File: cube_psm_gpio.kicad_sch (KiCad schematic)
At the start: 2 parts, among them J1 DF17_1.0H_-80DP-0.5V_57_

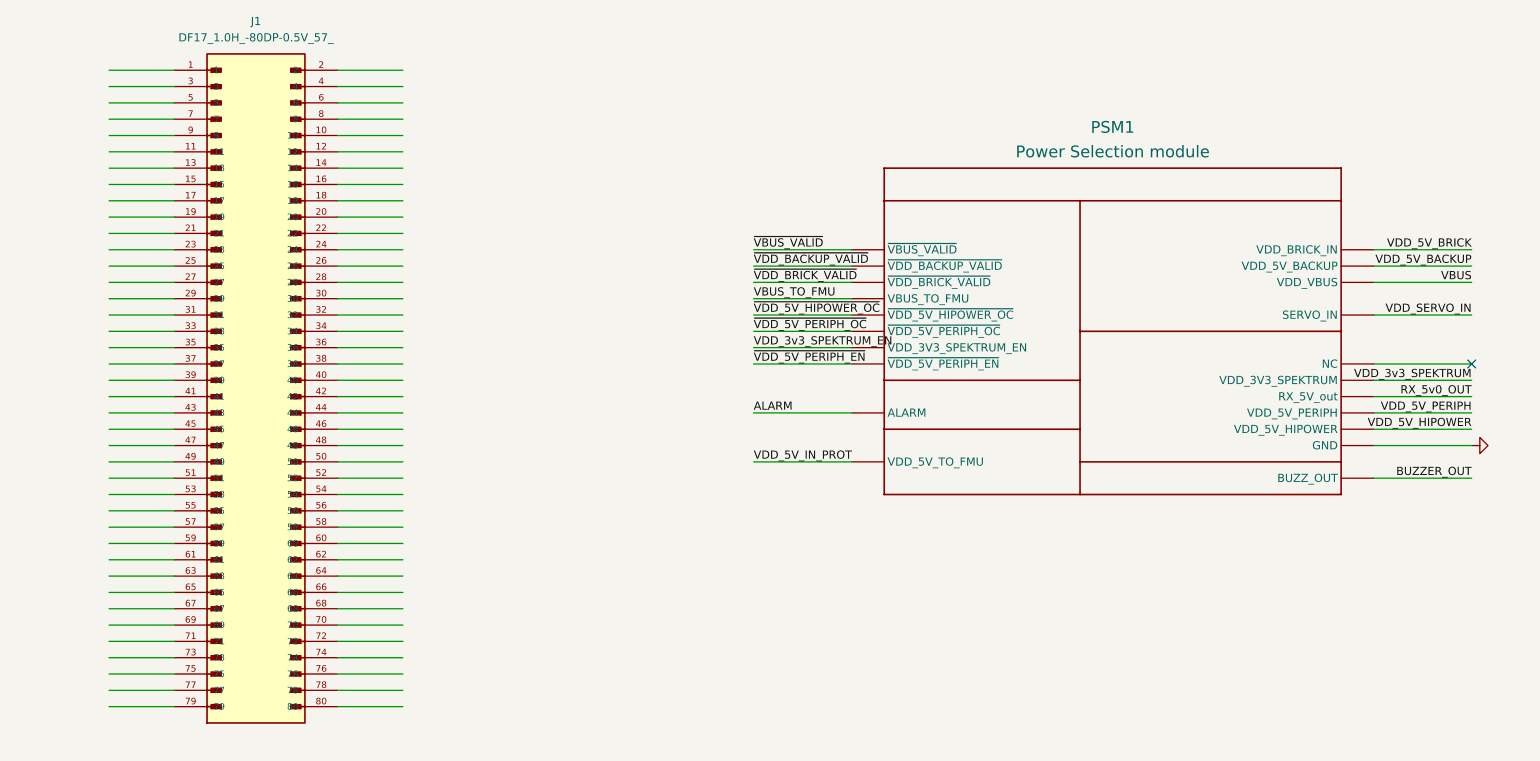
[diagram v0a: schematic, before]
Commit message: Connection for FC labelled
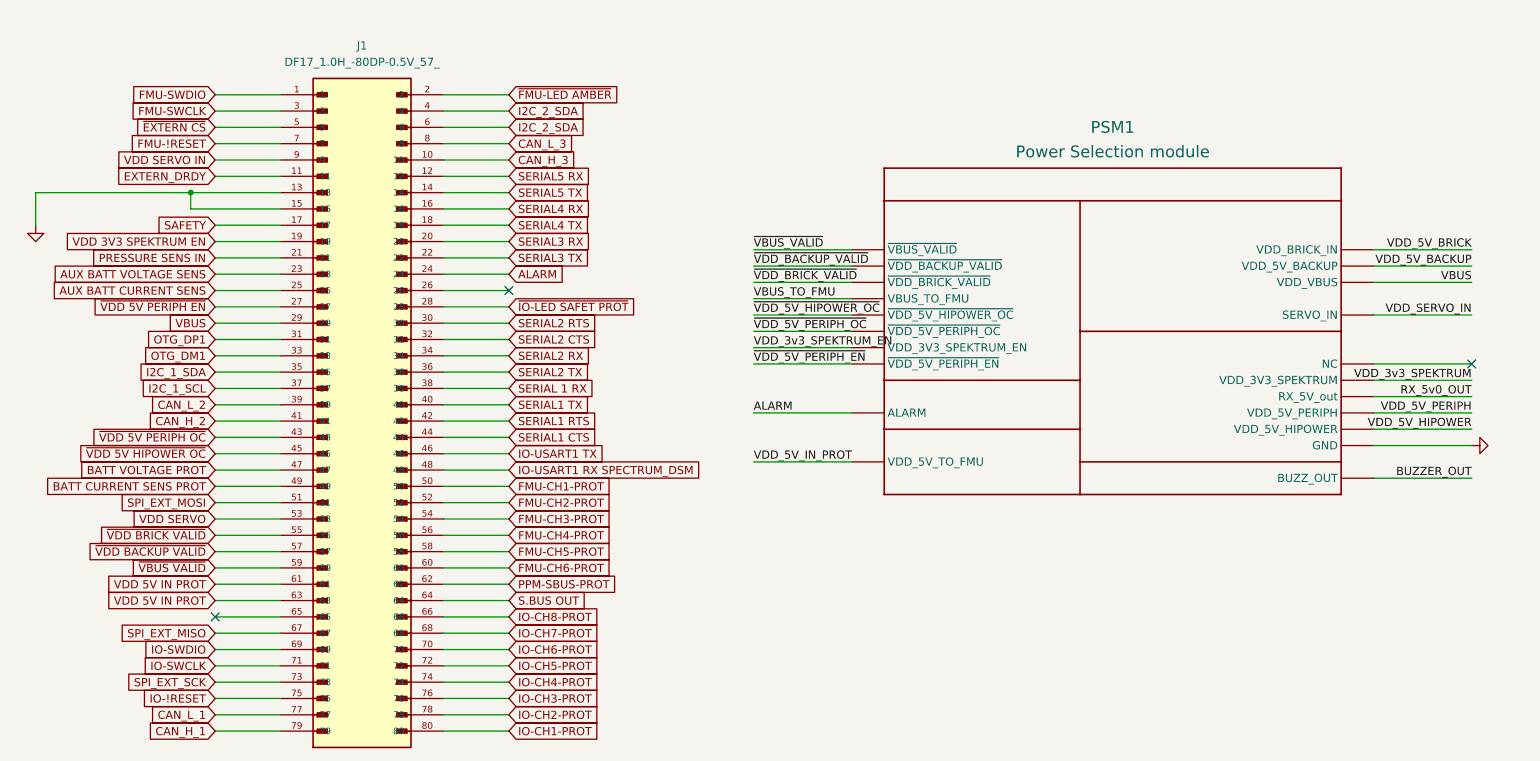
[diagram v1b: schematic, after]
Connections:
- net ALARM: now also J1.24
- net GND: now also J1.13, J1.15
- net VBUS: now also J1.29
- net FMU-SWDIO: now reaches J1.1
- net CAN_H_3: now reaches J1.10
- net EXTERN_DRDY: now reaches J1.11
- net SERIAL5 RX: now reaches J1.12
- net SERIAL5 TX: now reaches J1.14
- net SERIAL4 RX: now reaches J1.16
- net SAFETY: now reaches J1.17
- net SERIAL4 TX: now reaches J1.18
- net VDD 3V3 SPEKTRUM EN: now reaches J1.19
- net ~{FMU-LED AMBER}: now reaches J1.2
- net SERIAL3 RX: now reaches J1.20
- net PRESSURE SENS IN: now reaches J1.21
- net SERIAL3 TX: now reaches J1.22
- net AUX BATT VOLTAGE SENS: now reaches J1.23
- net AUX BATT CURRENT SENS: now reaches J1.25
- net ~{VDD 5V PERIPH EN}: now reaches J1.27
- net ~{IO-LED SAFET PROT}: now reaches J1.28
- net FMU-SWCLK: now reaches J1.3
- net SERIAL2 RTS: now reaches J1.30
- net OTG_DP1: now reaches J1.31
- net SERIAL2 CTS: now reaches J1.32
- net OTG_DM1: now reaches J1.33
- net SERIAL2 RX: now reaches J1.34
- net I2C_1_SDA: now reaches J1.35
- net SERIAL2 TX: now reaches J1.36
- net I2C_1_SCL: now reaches J1.37
- net SERIAL 1 RX: now reaches J1.38
- net CAN_L_2: now reaches J1.39
- net I2C_2_SDA: now reaches J1.4
- net I2C_2_SDA: now also J1.6
- net SERIAL1 TX: now reaches J1.40
- net CAN_H_2: now reaches J1.41
- net SERIAL1 RTS: now reaches J1.42
- net ~{VDD 5V PERIPH OC}: now reaches J1.43
- net SERIAL1 CTS: now reaches J1.44
- net ~{VDD 5V HIPOWER OC}: now reaches J1.45
- net IO-USART1 TX: now reaches J1.46
- net BATT VOLTAGE PROT: now reaches J1.47
- net IO-USART1 RX SPECTRUM_DSM: now reaches J1.48
- net BATT CURRENT SENS PROT: now reaches J1.49
- net ~{EXTERN CS}: now reaches J1.5
- net FMU-CH1-PROT: now reaches J1.50
- net SPI_EXT_MOSI: now reaches J1.51
- net FMU-CH2-PROT: now reaches J1.52
- net VDD SERVO: now reaches J1.53
- net FMU-CH3-PROT: now reaches J1.54
- net ~{VDD BRICK VALID}: now reaches J1.55
- net FMU-CH4-PROT: now reaches J1.56
- net ~{VDD BACKUP VALID}: now reaches J1.57
- net FMU-CH5-PROT: now reaches J1.58
- net ~{VBUS VALID}: now reaches J1.59
- net FMU-CH6-PROT: now reaches J1.60
- net VDD 5V IN PROT: now reaches J1.61
- net VDD 5V IN PROT: now also J1.63
- net PPM-SBUS-PROT: now reaches J1.62
- net S.BUS OUT: now reaches J1.64
- net IO-CH8-PROT: now reaches J1.66
- net SPI_EXT_MISO: now reaches J1.67
- net IO-CH7-PROT: now reaches J1.68
- net IO-SWDIO: now reaches J1.69
- net FMU-!RESET: now reaches J1.7
- net IO-CH6-PROT: now reaches J1.70
- net IO-SWCLK: now reaches J1.71
- net IO-CH5-PROT: now reaches J1.72
- net SPI_EXT_SCK: now reaches J1.73
- net IO-CH4-PROT: now reaches J1.74
- net IO-!RESET: now reaches J1.75
- net IO-CH3-PROT: now reaches J1.76
- net CAN_L_1: now reaches J1.77
- net IO-CH2-PROT: now reaches J1.78
- net CAN_H_1: now reaches J1.79
- net CAN_L_3: now reaches J1.8
- net IO-CH1-PROT: now reaches J1.80
- net VDD SERVO IN: now reaches J1.9
- no-connect marks 1 -> 3
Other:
- moved on the sheet: J1

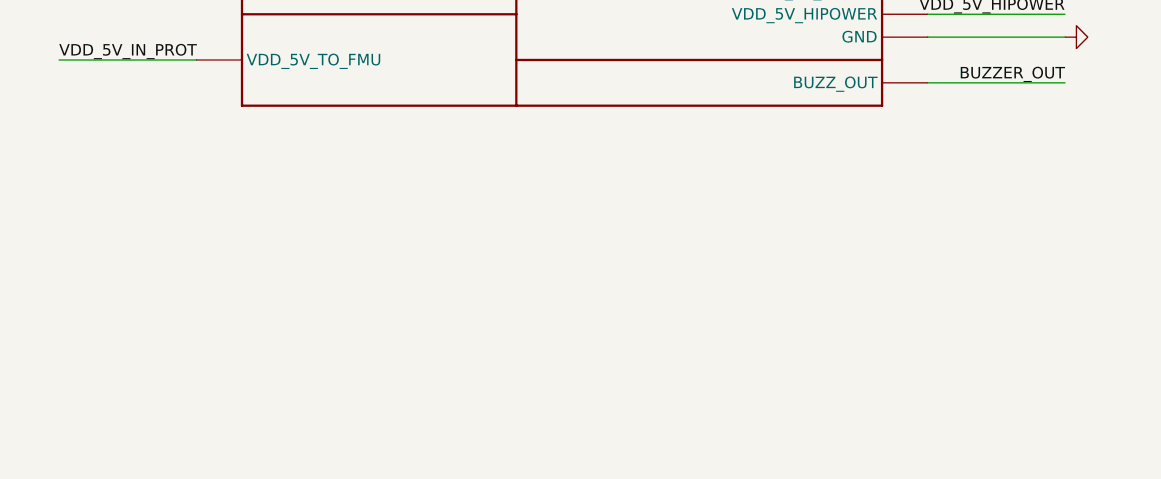
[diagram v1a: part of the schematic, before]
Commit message: Added power plugs, still need decide whether power with come from the PI or separate source
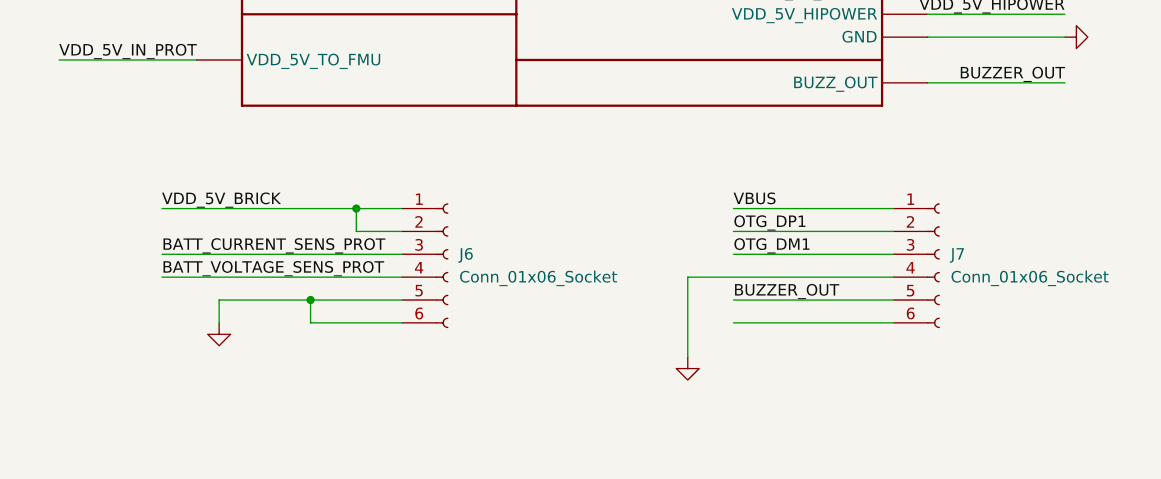
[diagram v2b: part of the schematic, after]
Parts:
- added J6, J7: Conn_01x06_Socket, symbol Connector:Conn_01x06_Socket
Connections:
- net BUZZER_OUT: now also J7.5 (Pin_5)
- net GND: now also J6.5 (Pin_5), J6.6 (Pin_6), J7.4 (Pin_4)
- net OTG_DM1: now also J7.3 (Pin_3)
- net OTG_DP1: now also J7.2 (Pin_2)
- net VBUS: now also J7.1 (Pin_1)
- net VDD_5V_BRICK: now also J6.1 (Pin_1), J6.2 (Pin_2)
- new net BATT_CURRENT_SENS_PROT: J6.3 (Pin_3)
- new net BATT_VOLTAGE_SENS_PROT: J6.4 (Pin_4)

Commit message: PCB Layout edited
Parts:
- J6, J7: footprint (none) -> Connector_Molex:Molex_MicroClasp_55932-0630_1x06_P2.00mm_Vertical
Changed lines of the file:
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@@
 			)
 		)
-		(property "Footprint" ""
+		(property "Footprint" "Connector_Molex:Molex_MicroClasp_55932-0630_1x06_P2.00mm_Vertical"
 			(at 172.72 113.03 0)
 			(effects
@@
 			)
 		)
-		(property "Footprint" ""
+		(property "Footprint" "Connector_Molex:Molex_MicroClasp_55932-0630_1x06_P2.00mm_Vertical"
 			(at 227.33 113.03 0)
 			(effects
